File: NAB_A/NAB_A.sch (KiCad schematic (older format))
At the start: 38 parts, among them K1 кнопка, K2 кнопка, X1 Check_point

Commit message: NAB_A: готова трассировка, требуется проверка и дополнить трассировку
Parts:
- removed R7, R8: Резистор_0,065Вт, N_RLC:Резистор_SMD_0603_0,065_Вт, symbol elements:Резистор_0,065Вт
- removed VT1: Транзистор_полевой_P-канал(IRLML2246TRPBF), N_VD_HL:Транзистор_IRLML6344TR_SOT-23, symbol elements:Транзистор_полевой_P-канал(IRLML2246TRPBF)
- removed XP1: Вилка_PLS4, N_X:Вилка_PLS4_вертикальная, symbol elements:Вилка_PLS4
- added BK1: Преобразователь_температуры_LM75AD, N_DD:SO-8, symbol elements_2020:Преобразователь_температуры_LM75AD
- added LOGO1: LOGO, N_ICO:ni_10x10, symbol elements_2020:LOGO
- added R11, R12, R13, R14: Резистор_0,065Вт, N_RLC:Резистор_SMD_0603_0,065_Вт, symbol elements:Резистор_0,065Вт
- added VT2: Транзистор_полевой_P-канал(IRLML2246TRPBF), N_VD_HL:Транзистор_IRLML6344TR_SOT-23, symbol elements:Транзистор_полевой_P-канал(IRLML2246TRPBF)
- added XP4: Вилка_PLS5, N_X:Вилка_угловая_XH.254_5, symbol elements:Вилка_PLS5
- added XP5: Вилка_PLS2, N_X:Вилка_PLS2_вертикальная, symbol elements:Вилка_PLS2
- added XS2: Розетка_PBS3, N_X:Розетка_PBS3_вертикальная, symbol elements:Розетка_PBS3
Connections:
- net DATA is gone; now on net TX_DATA: XS1.3
- net 5V: now also XP4.1, XP4.5; no longer R9.2, XP3.2 (VCC)
- net CHARGE_STATUS: now also DD1.2 (PD4(XCK/T0))
- net GND: now also DD1.21 (GND), DD1.3 (GND), DD1.5 (GND), BK1.4 (GND), BK1.5 (A2), BK1.6 (A1), BK1.7 (A0), R13.2, XP4.3, XP5.2, XS2.1
- net MC_RX: now also DD1.30 (PD0(RXD)), XP4.4
- net MC_TX: now also DD1.31 (PD1(TXD)), XP4.2
- net MC_VCC: now also DD1.18 (AVCC), DD1.4 (VCC), DD1.6 (VCC), R9.2, XP3.2 (VCC), BK1.8 (VCC), R11.1, R12.1, XS2.2
- net MISO: now also DD1.16 (PB4(MISO))
- net MOSI: now also DD1.15 (PB3(MOSI/OC2))
- net SCK: now also DD1.17 (PB5(SCK))
- net SCL: now also DD1.28 (PC5(ADC5/SCL)), BK1.2 (SCL), R12.2
- net SDA: now also DD1.27 (PC4(ADC4/SDA)), BK1.1 (SDA), R11.2
- net V_BAT: now also R14.1, VT2.2
- net nRESET: now also DD1.29 (PC6(RESET))
- net BUT-2: now reaches DD1.1 (PD3(INT1))
- net BUT-2: now also K2.1
- net HL-2: now reaches DD1.10 (PD6(AIN0))
- net HL-2: now also R2.1
- net HL-3: now reaches DD1.11 (PD7(AIN1))
- net HL-3: now also R3.1
- net HL-4: now reaches DD1.12 (PB0(ICP1))
- net HL-4: now also R4.1
- net HL-5: now reaches DD1.13 (PB1(OC1A))
- net HL-5: now also R5.1
- net DTH_DATA: now reaches DD1.14 (PB2(SS/OC1B))
- net DTH_DATA: now also XS2.3
- net BUT-1: now reaches DD1.32 (PD2(INT0))
- net BUT-1: now also K1.1
- net TX_DATA: now reaches DD1.7 (PB6(XTAL1/TOSC1))
- net HL-1: now reaches DD1.9 (PD5(T1))
- net HL-1: now also R1.1
- net QI-1: now reaches VD1.3, VD3.1, VD3.2, XP2.1
- net QI-2: now reaches VD2.3, VD4.1, VD4.2, XP2.2
- net QI+: now reaches L1.1, VD3.3, VD4.3
- new net: R13.1, R14.2, VT2.1
- new net BAT_IN: VT2.3, XP5.1
- no-connect marks 1 -> 9
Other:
- note added: "Антенна Qi"
- note added: "Внешний аккум"
- note added: "Модуль передатчика\n433 МГц"
- note added: "Модуль температуры\nи влажности"
- moved on the sheet: C3, C5, C6, C7, HL1, HL2, HL3, HL4, HL5, K1, K2, L1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

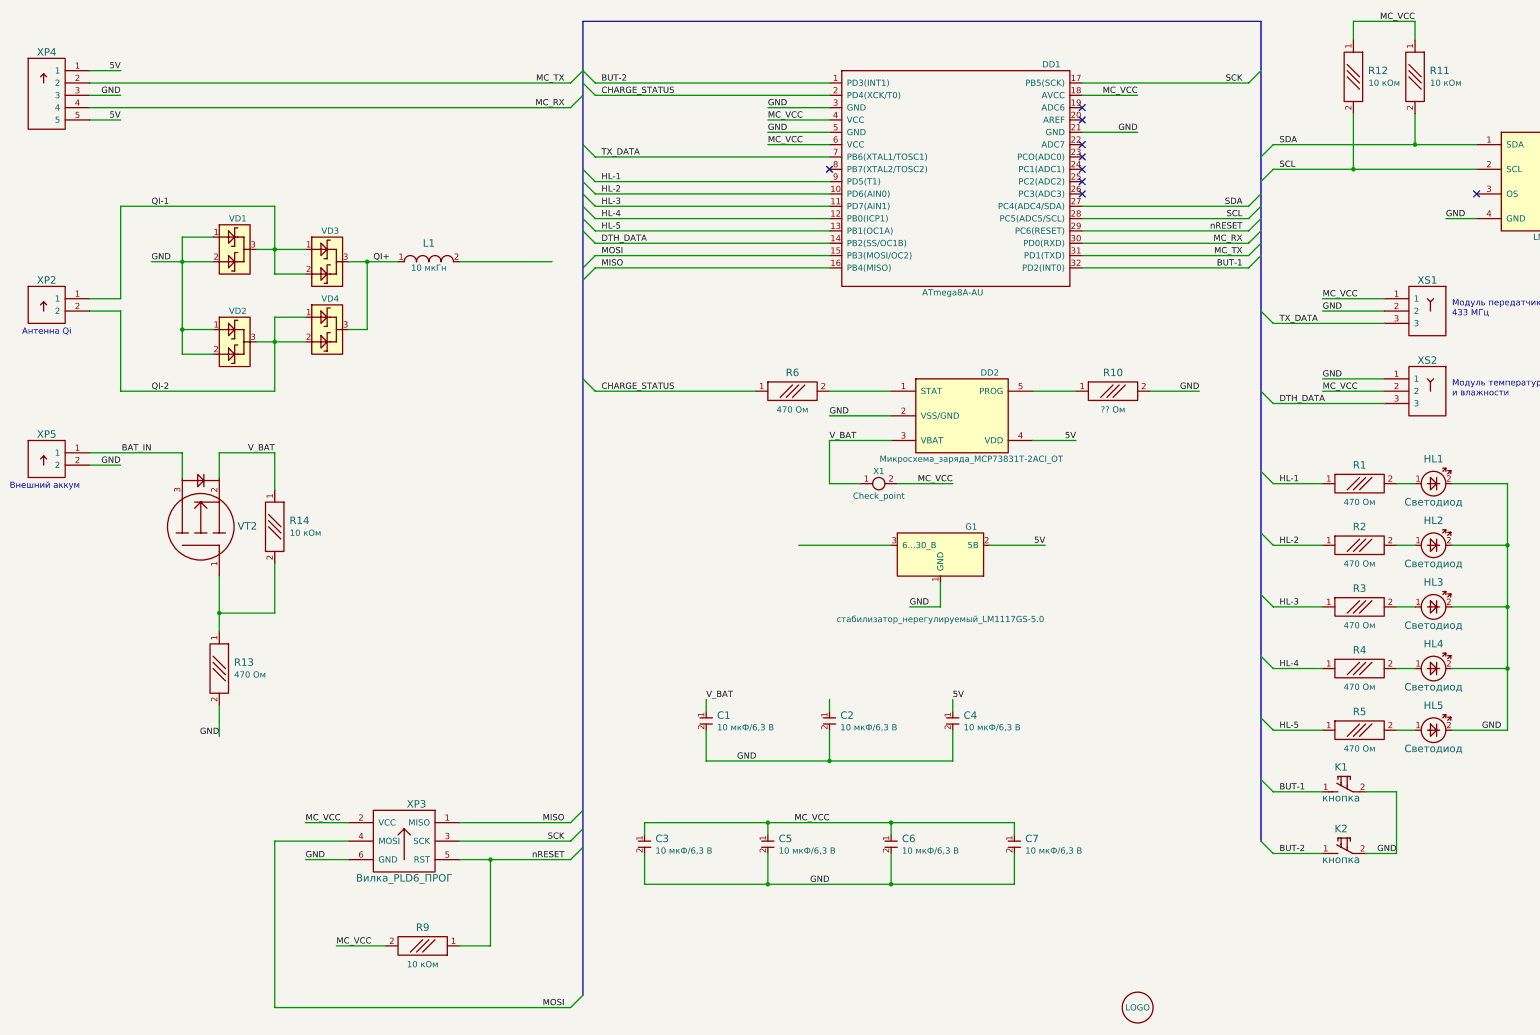
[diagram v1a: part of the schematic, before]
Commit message: NAB_A: 433data перенесен на uart-tx, заведена аналоговая часть, +silk
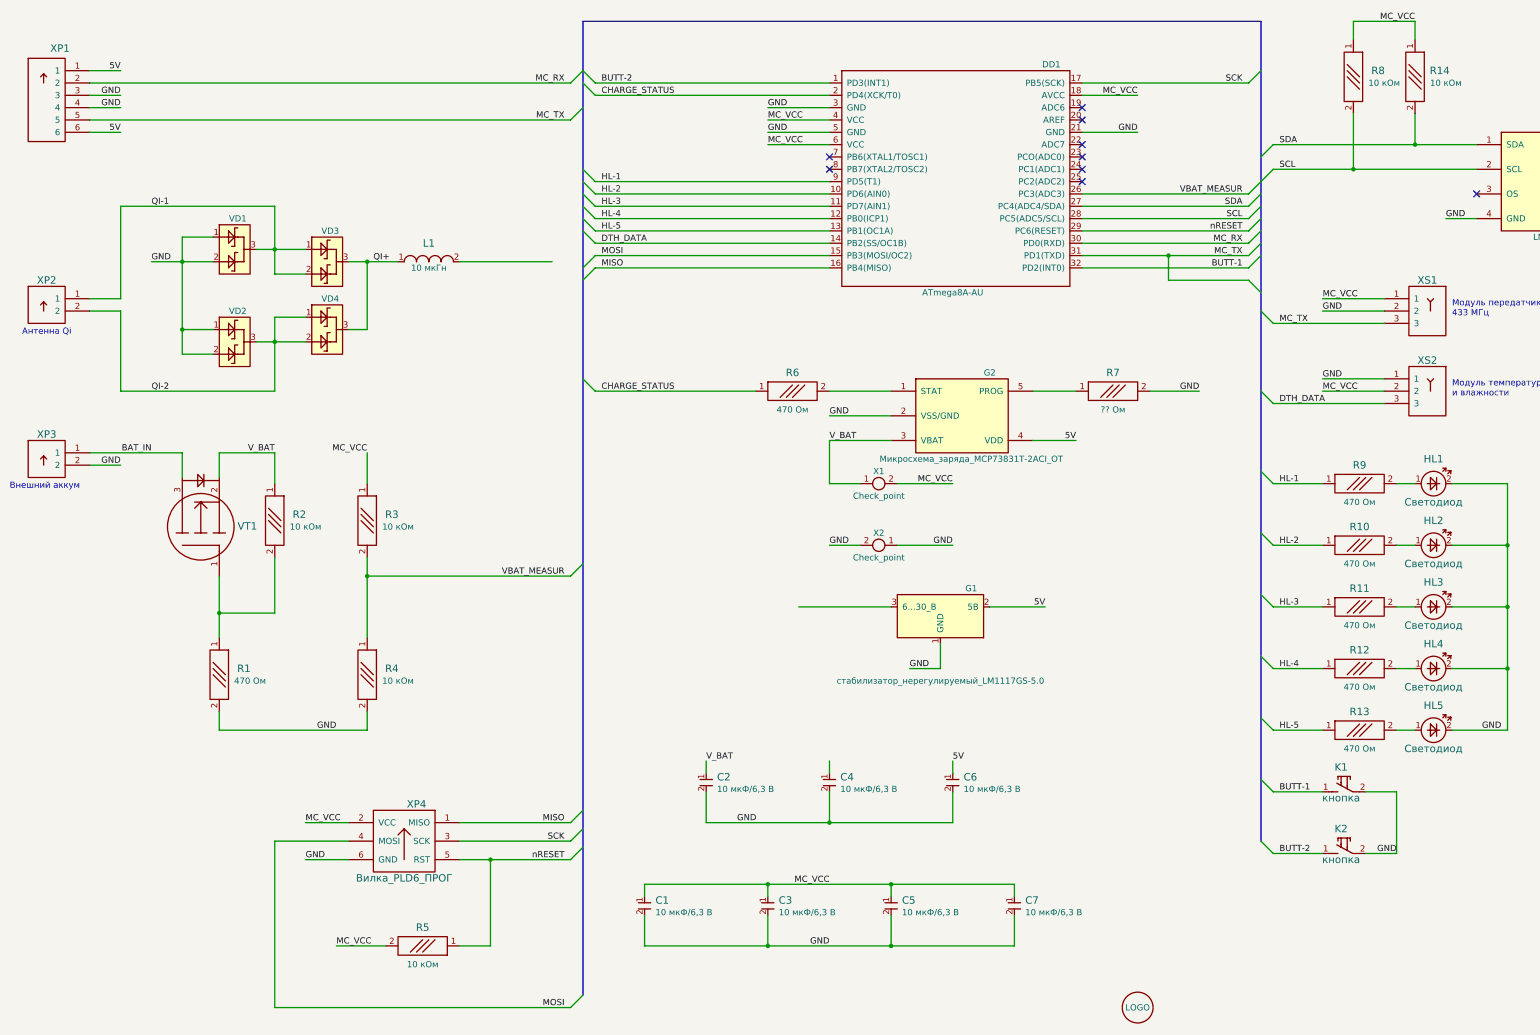
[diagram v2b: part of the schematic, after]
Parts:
- removed XP4: Вилка_PLS5, N_X:Вилка_угловая_XH.254_5, symbol elements:Вилка_PLS5
- added R3, R4: Резистор_0,065Вт, N_RLC:Резистор_SMD_0603_0,065_Вт, symbol elements:Резистор_0,065Вт
- added X2: Check_point, N_X:Пробник, symbol elements_2020:Check_point
- added XP1: Вилка_PLS6, N_X:Вилка_PLS6_вертикальная, symbol elements:Вилка_PLS6
- renumbered C3 to C1, C1 to C2, C5 to C3, C2 to C4, C6 to C5, C4 to C6, DD2 to G2, R13 to R1, R2 to R10, R3 to R11, R4 to R12, R5 to R13, R11 to R14, R14 to R2, R9 to R5, R10 to R7, R12 to R8, R1 to R9, VT2 to VT1, XP5 to XP3, XP3 to XP4
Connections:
- net 5V: now also XP1.1, XP1.6
- net GND: now also R4.2, X2.1, X2.2, XP1.3, XP1.4
- net MC_RX: now also XP1.2
- net MC_TX: now also XS1.3, XP1.5
- net MC_VCC: now also R3.1
- net VBAT_MEASUR: now reaches DD1.26 (PC3(ADC3))
- net VBAT_MEASUR: now also R3.2, R4.1
- net BUT-1 renamed BUTT-1
- net BUT-2 renamed BUTT-2
- net TX_DATA: no longer names the net of DD1.7 (PB6(XTAL1/TOSC1))
- net TX_DATA: no longer XS1.3
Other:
- moved on the sheet: C1, C2, C3, C4, C5, C6, C7, G1, R1, R2
